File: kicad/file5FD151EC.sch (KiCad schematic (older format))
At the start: 5 parts, among them J3 Conn_ARM_JTAG_SWD_10

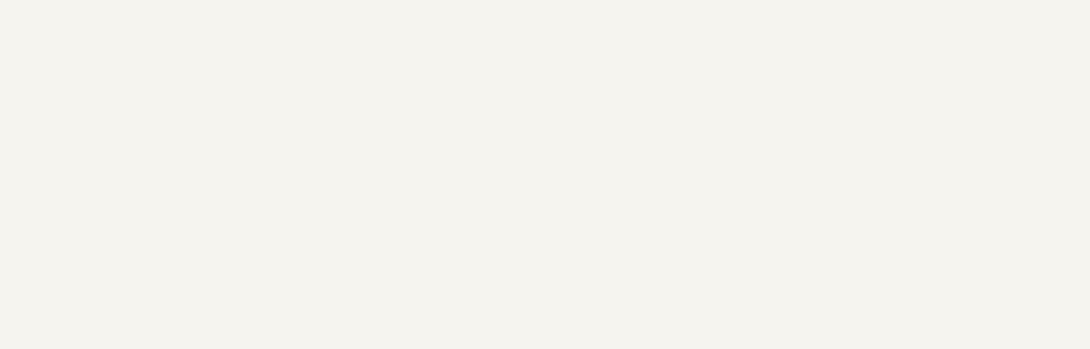
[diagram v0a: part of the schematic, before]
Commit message: Power reg U2/U3 and supporting components
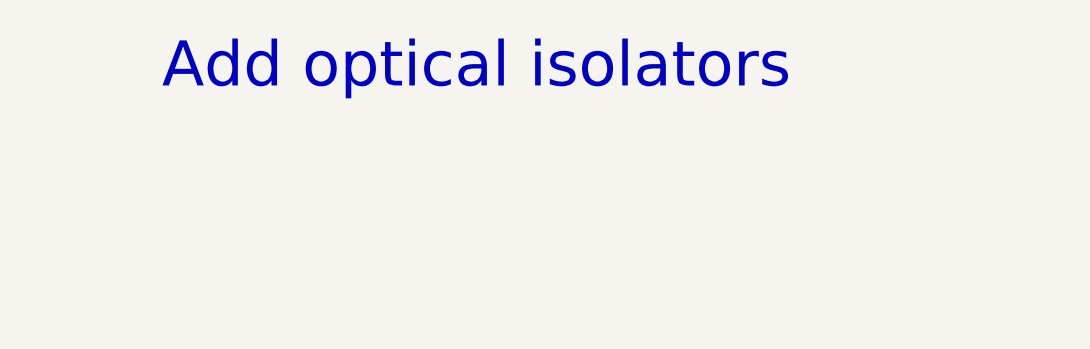
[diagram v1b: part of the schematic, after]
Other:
- note added: "Add optical isolators"
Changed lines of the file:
@@
 Text HLabel 7200 4350 2    50   Output ~ 0
 TDI
+Text Notes 7900 2650 0    197  ~ 0
+Add optical isolators
 $EndSCHEMATC
